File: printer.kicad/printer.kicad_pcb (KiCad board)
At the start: 2 copper layers, 74 x 47 mm, 34 parts, among them J1 ZX_Spectrum_128K_expansion, J2 Conn_01x06_Male, J3 Conn_01x05_Male, J4 Conn_01x04_Male, U1 SN74AHC373, U2 SN74HCT00, U3 SN74AHCT02, U4 SN74AHC373, U5 XC6206PxxxMR, U6 STM32F103C8Tx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

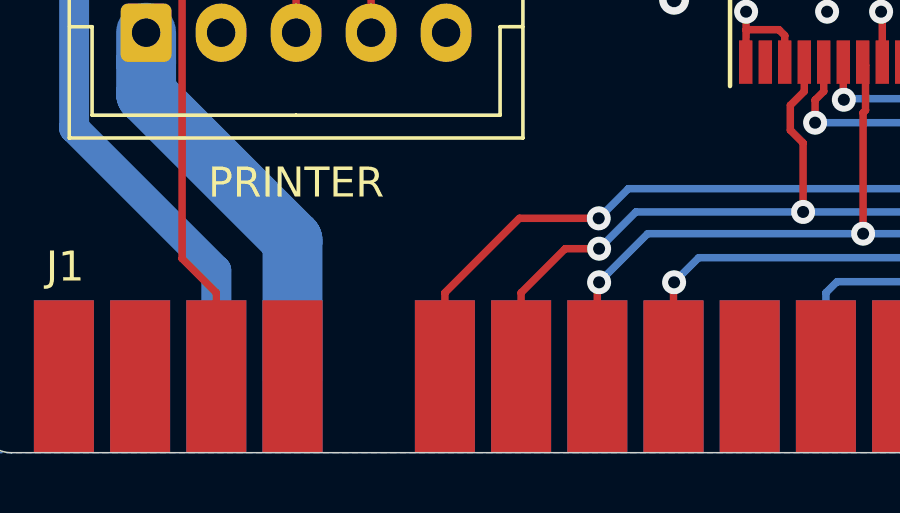
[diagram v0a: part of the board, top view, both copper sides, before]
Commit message: Add thicker connection of the ground plane
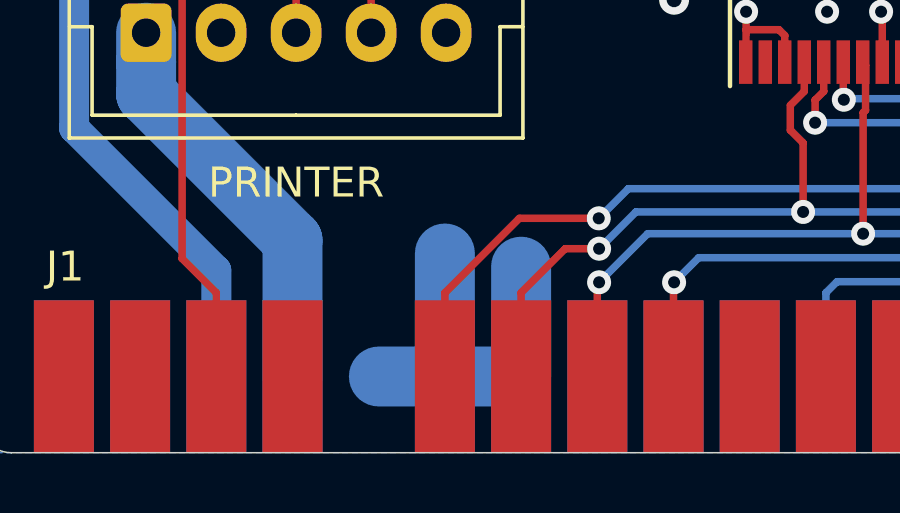
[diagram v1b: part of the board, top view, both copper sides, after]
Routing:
- net GND: track 94.5 -> 107.0 mm
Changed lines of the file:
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@@
     (thickness 1.6)
     (drawings 21)
-    (tracks 605)
+    (tracks 608)
     (zones 0)
     (modules 34)
@@
   )
   (setup
-    (last_trace_width 0.25)
+    (last_trace_width 2)
     (user_trace_width 0.5)
     (user_trace_width 1)
@@
   (segment (start 141.2 96.8) (end 139.8 96.8) (width 0.25) (layer F.Cu) (net 1))
   (via (at 151.02499 97.07501) (size 0.8) (drill 0.4) (layers F.Cu B.Cu) (net 1) (status 1000000))
+  (segment (start 124.46 124.46) (end 124.46 120.36) (width 2) (layer B.Cu) (net 1))
+  (segment (start 127 124.46) (end 127 120.8) (width 2) (layer B.Cu) (net 1))
+  (segment (start 127 124.46) (end 122.26 124.46) (width 2) (layer B.Cu) (net 1))
   (segment (start 134.339999 108.204) (end 134.463999 108.08) (width 0.5) (layer F.Cu) (net 2))
   (segment (start 132.1 108.204) (end 134.339999 108.204) (width 0.5) (layer F.Cu) (net 2))

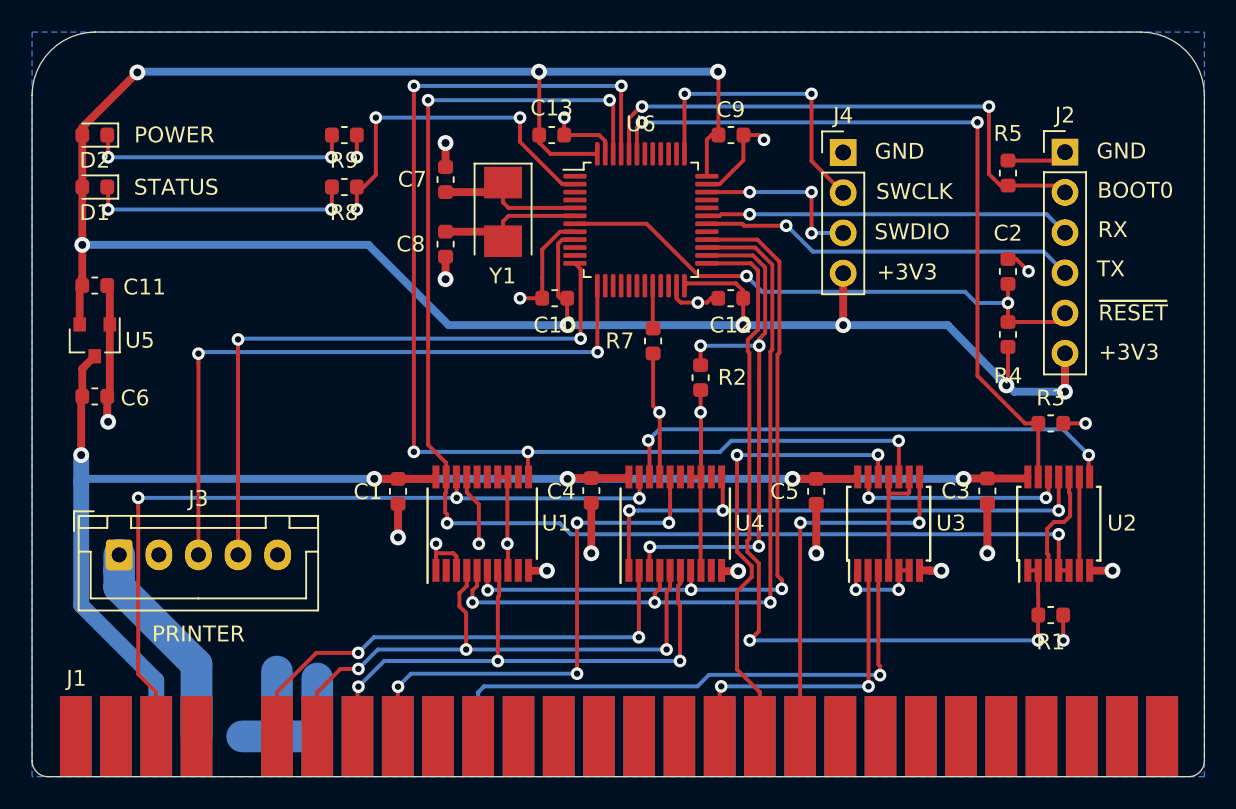
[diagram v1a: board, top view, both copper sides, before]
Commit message: Add unconnected copper pour to top side
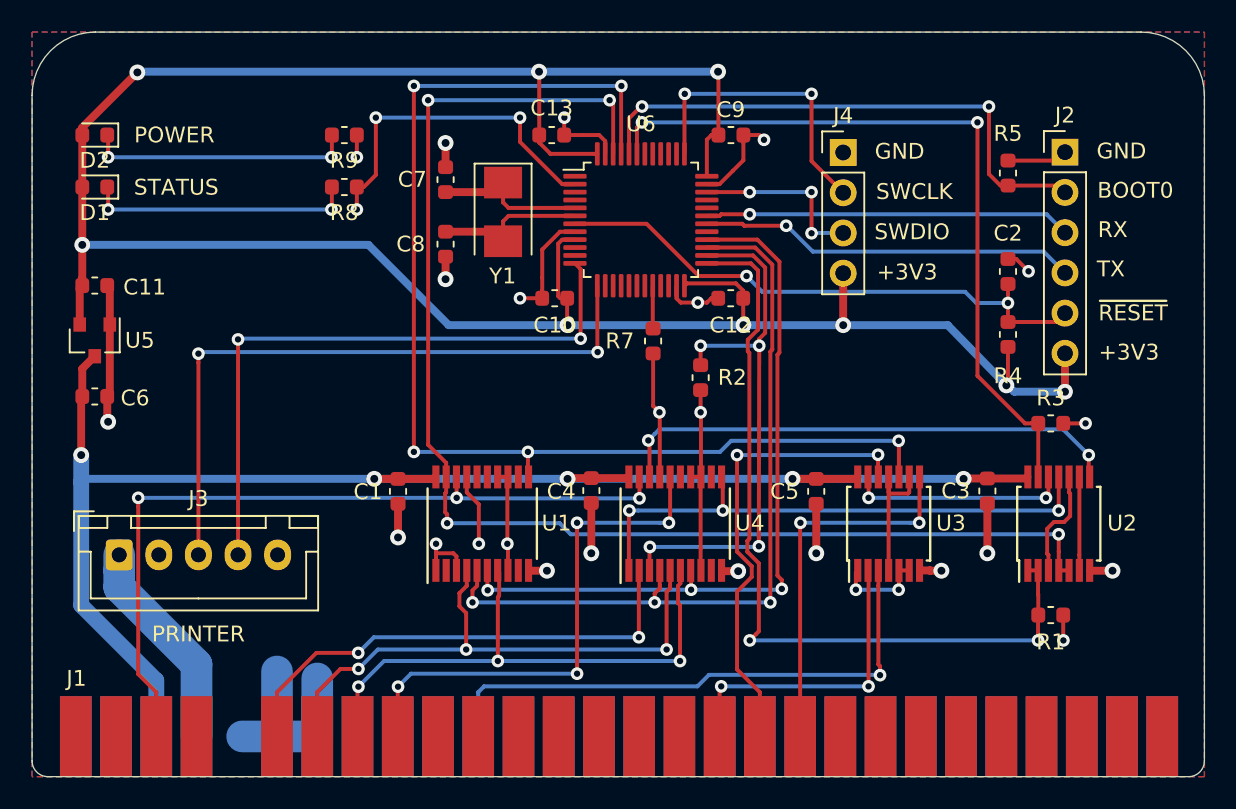
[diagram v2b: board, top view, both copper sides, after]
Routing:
- added copper zone on F.Cu, net (none)
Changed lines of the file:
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@@
   )
   (setup
-    (last_trace_width 2)
+    (last_trace_width 0.25)
     (user_trace_width 0.5)
     (user_trace_width 1)
@@
     (connect_pads (clearance 0.508))
     (min_thickness 0.254)
+    (fill yes (arc_segments 32) (thermal_gap 0.508) (thermal_bridge_width 0.508))
+    (polygon
+      (pts
+        (xy 183 127) (xy 109 127) (xy 109 80) (xy 183 80)
+      )
+    )
+  )
+  (zone (net 0) (net_name "") (layer F.Cu) (hatch edge 0.508)
+    (connect_pads (clearance 0.508))
+    (min_thickness 0.254)
